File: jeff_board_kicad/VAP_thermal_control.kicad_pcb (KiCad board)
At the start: 2 copper layers, 63.5 x 81.3 mm, 32 parts, among them J1 Conn_01x02_Female, J2 Conn_01x02_Female, J3 Conn_01x02_Female, Q1 IRLB8721PBF, Q2 IRLB8721PBF, U1 TSR_1-24150, U2 MAX31865Breakout, U3 MLX90614, U4 MIC4427

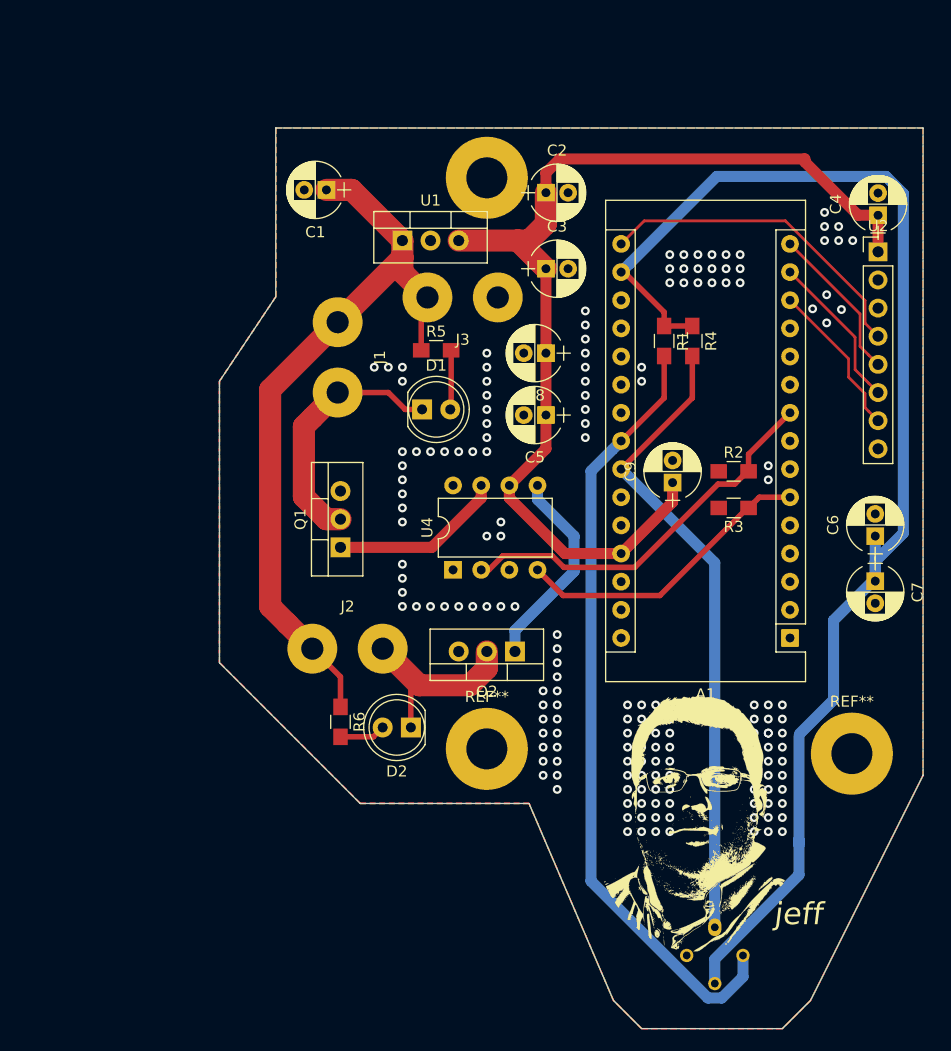
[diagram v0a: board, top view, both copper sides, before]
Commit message: Prelim Layout of jeff V2
Added two channels of PWM, so we can drive 4 of (Fan/Heater/LEDs).
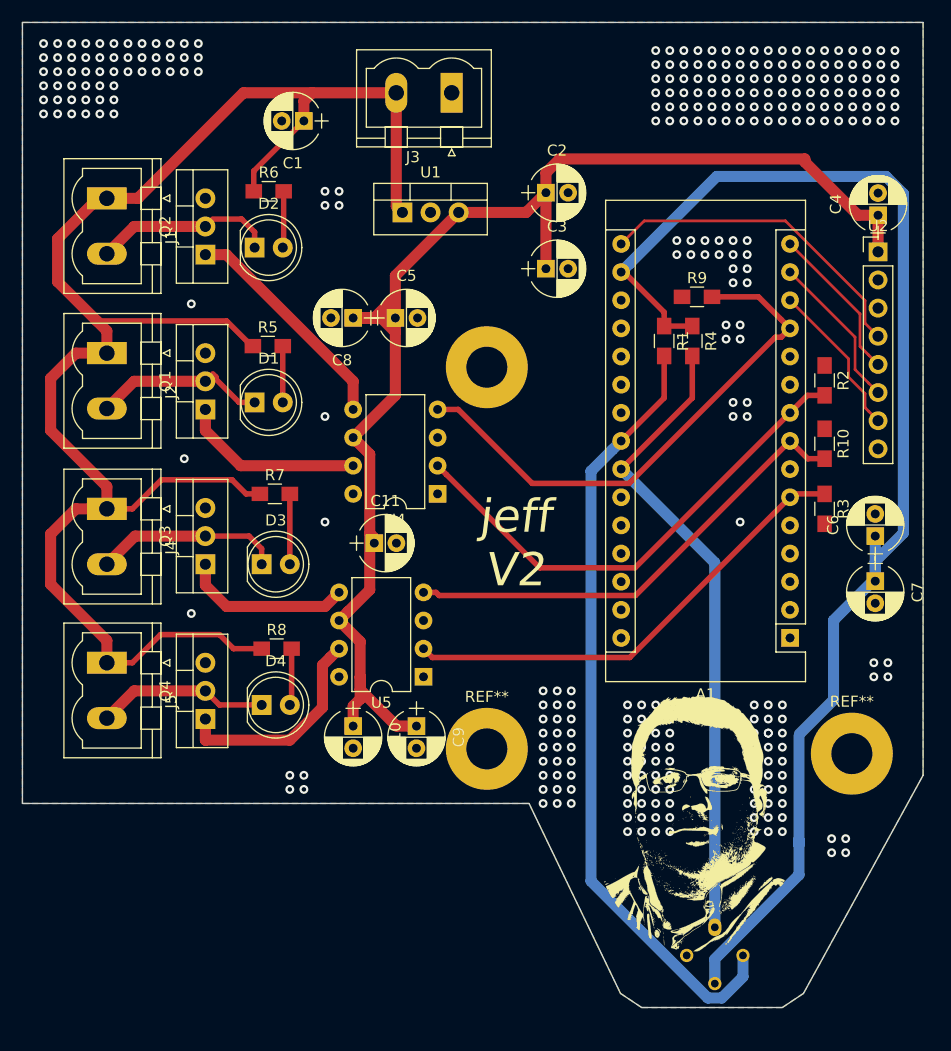
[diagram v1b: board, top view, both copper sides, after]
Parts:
- added C10: 0.1u, Capacitors_THT:CP_Radial_D5.0mm_P2.00mm, F.Cu at (60.3, 122.6)
- added C11: 1u, Capacitors_THT:CP_Radial_D5.0mm_P2.00mm, F.Cu at (62.2, 106.0)
- added D3: LED, LEDs:LED_D5.0mm, F.Cu at (52.1, 108.0)
- added D4: LED, LEDs:LED_D5.0mm, F.Cu at (52.1, 120.7)
- added J4: Conn_01x02_Female, Connectors_Phoenix:PhoenixContact_MSTBVA-G_02x5.00mm_Vertical, F.Cu at (38.1, 103.0)
- added J5: Conn_01x02_Female, Connectors_Phoenix:PhoenixContact_MSTBVA-G_02x5.00mm_Vertical, F.Cu at (38.1, 116.8)
- added Q3: IRLB8721PBF, TO_SOT_Packages_THT:TO-220-3_Vertical, F.Cu at (47.0, 108.0)
- added Q4: IRLB8721PBF, TO_SOT_Packages_THT:TO-220-3_Vertical, F.Cu at (47.0, 121.9)
- added R10: 10k, Resistors_SMD:R_0805_HandSoldering, F.Cu at (102.9, 97.1)
- added R7: 1k, Resistors_SMD:R_0805_HandSoldering, F.Cu at (53.3, 101.6)
- added R8: 1k, Resistors_SMD:R_0805_HandSoldering, F.Cu at (53.4, 115.6)
- added R9: 10k, Resistors_SMD:R_0805_HandSoldering, F.Cu at (91.4, 83.8)
- added U5: MIC4427, Housings_DIP:DIP-8_W7.62mm, F.Cu at (66.7, 118.1)
- J1, J2, J3: footprint Wire_Pads:SolderWirePad_2x_2mmDrill -> Connectors_Phoenix:PhoenixContact_MSTBVA-G_02x5.00mm_Vertical
- moved R6 48.3 mm to (52.7, 74.3), turned to 0 degrees
- moved D2 45.5 mm to (51.4, 79.4), turned to 0 degrees
- moved Q2 45.4 mm to (47.0, 80.0), turned to 90 degrees
- moved J2 34.4 mm to (38.1, 88.9), turned to 270 degrees
- moved C9 31.9 mm to (66.0, 122.6), turned to 270 degrees
- moved J1 25.3 mm to (38.1, 74.9)
- moved J3 18.5 mm to (69.2, 65.4)
- moved C8 17.7 mm to (60.3, 85.7)
- moved Q1 17.4 mm to (47.0, 94.0)
- moved REF** 17.1 mm to (72.4, 90.2)
- moved C5 16.2 mm to (64.1, 85.7), turned to 0 degrees
- moved R5 15.2 mm to (52.6, 88.3)
- moved D1 15.1 mm to (51.4, 93.3)
- moved R2 11.6 mm to (102.9, 91.4), turned to 270 degrees
- moved R3 8.21 mm to (102.9, 103.0), turned to 270 degrees
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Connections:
- A1 pad 27: +5V -> Net-(A1-Pad27)
- A1 pad 30: Net-(A1-Pad30) -> +5V
- R3 pad 1: Net-(A1-Pad6) -> Net-(A1-Pad12)
- U4 pad 4: Net-(A1-Pad6) -> Net-(A1-Pad12)
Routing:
- net +24V: track 68.0 -> 155.9 mm
- net Net-(A1-Pad12): track 0.00 -> 48.6 mm
- net Net-(A1-Pad8): track 0.00 -> 42.8 mm
- net +5V: track 95.3 -> 127.8 mm
- net Net-(Q4-Pad1): track 0.00 -> 19.6 mm
- net Net-(D3-Pad1): track 0.00 -> 16.9 mm
- net Net-(D4-Pad1): track 0.00 -> 15.5 mm
- net Net-(Q3-Pad1): track 0.00 -> 15.3 mm
- net Net-(A1-Pad6): track 27.4 -> 42.6 mm
- net Net-(A1-Pad9): track 35.5 -> 45.2 mm
- net Net-(D1-Pad1): track 23.1 -> 14.9 mm
- net Net-(D3-Pad2): track 0.00 -> 6.35 mm
- net Net-(D2-Pad1): track 21.1 -> 15.6 mm
- net Net-(D4-Pad2): track 0.00 -> 5.15 mm
- net Net-(Q2-Pad1): track 18.6 -> 20.6 mm
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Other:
- board size 63.5 x 81.3 mm -> 81.3 x 88.9 mm
- board text added: "jeff V2"
- board text removed: "jeff"
